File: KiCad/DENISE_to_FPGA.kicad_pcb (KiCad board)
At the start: 2 copper layers, 100 x 26.9 mm, 19 parts, among them J1 Conn_01x02, J2 Conn_01x02, J3 Conn_01x40, U1 LM1117-3.3, U2 74LVC162244A, U3 74LVC1G57GV, U4 Denise_MB_PinHeader

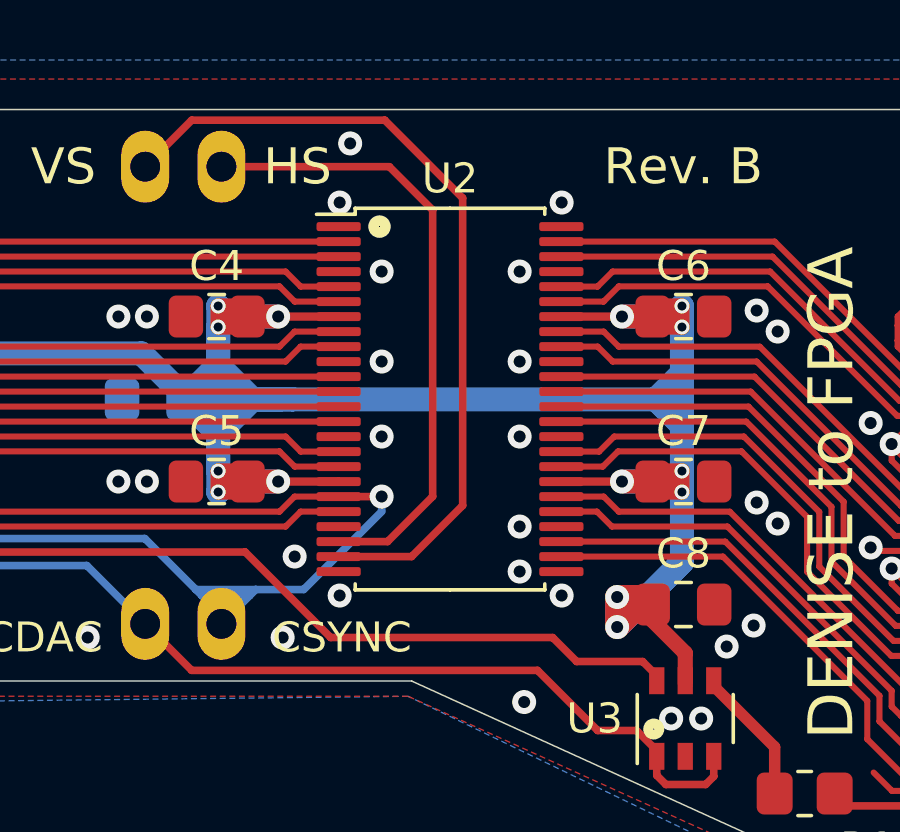
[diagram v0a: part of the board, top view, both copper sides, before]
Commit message: Fixed orientation of U2
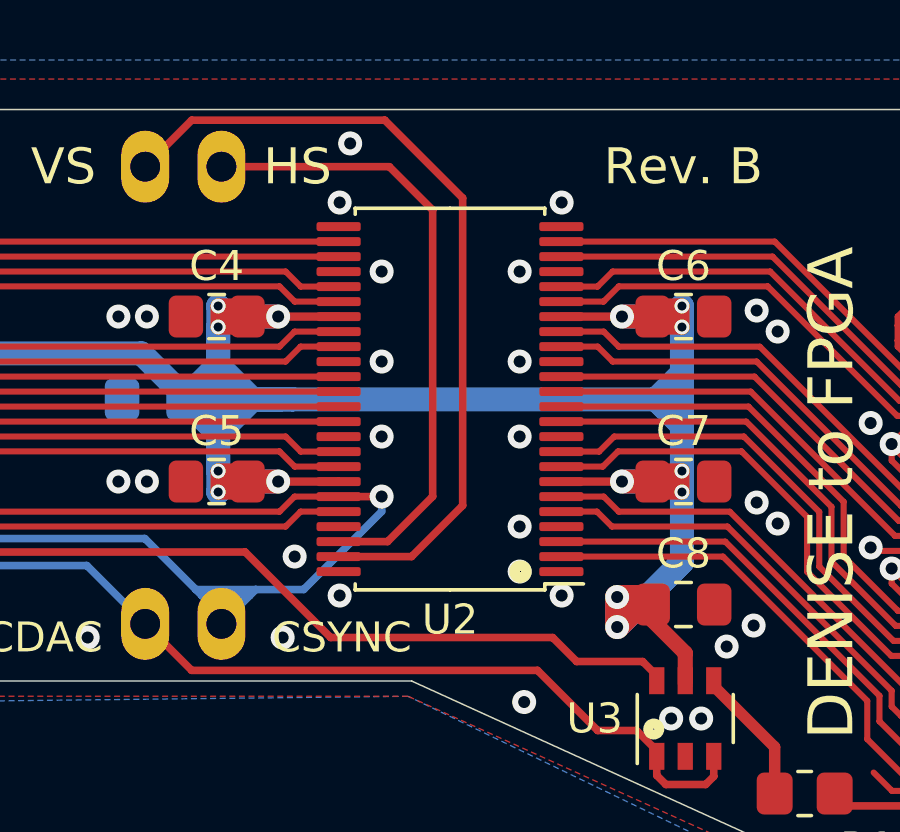
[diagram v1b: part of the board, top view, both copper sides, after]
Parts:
- turned U2 to 180 degrees
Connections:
- U2 pad 11: G2 -> B1_3V3
- U2 pad 12: G3 -> B0_3V3
- U2 pad 13: B0 -> G3_3V3
- U2 pad 14: B1 -> G2_3V3
- U2 pad 16: B2 -> G1_3V3
- U2 pad 17: B3 -> G0_3V3
- U2 pad 19: CSYNC -> R3_3V3
- U2 pad 2: R0 -> VSYNC_3V3
- U2 pad 20: PIXELSW -> R2_3V3
- U2 pad 22: HSYNC -> R1_3V3
- U2 pad 23: VSYNC -> R0_3V3
- U2 pad 26: VSYNC_3V3 -> R0
- U2 pad 27: HSYNC_3V3 -> R1
- U2 pad 29: PIXELSW_3V3 -> R2
- U2 pad 3: R1 -> HSYNC_3V3
- U2 pad 30: CSYNC_3V3 -> R3
- U2 pad 32: B3_3V3 -> G0
- U2 pad 33: B2_3V3 -> G1
- U2 pad 35: B1_3V3 -> G2
- U2 pad 36: B0_3V3 -> G3
- U2 pad 37: G3_3V3 -> B0
- U2 pad 38: G2_3V3 -> B1
- U2 pad 40: G1_3V3 -> B2
- U2 pad 41: G0_3V3 -> B3
- U2 pad 43: R3_3V3 -> CSYNC
- U2 pad 44: R2_3V3 -> PIXELSW
- U2 pad 46: R1_3V3 -> HSYNC
- U2 pad 47: R0_3V3 -> VSYNC
- U2 pad 5: R2 -> PIXELSW_3V3
- U2 pad 6: R3 -> CSYNC_3V3
- U2 pad 8: G0 -> B3_3V3
- U2 pad 9: G1 -> B2_3V3
